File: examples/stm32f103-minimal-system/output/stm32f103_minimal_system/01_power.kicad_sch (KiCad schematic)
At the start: 8 parts, among them J1 USB-C16PIN, U2 AMS1117-3.3

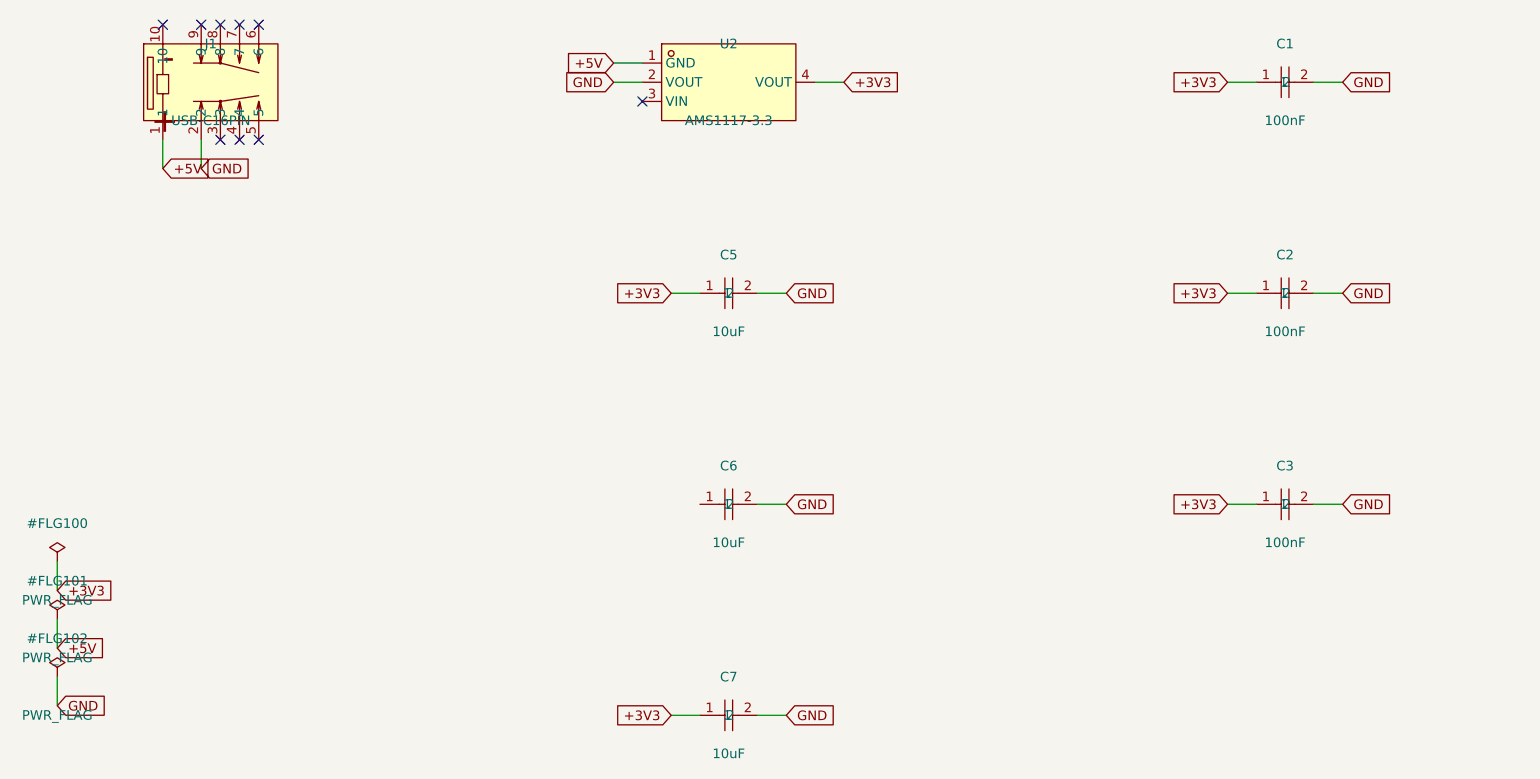
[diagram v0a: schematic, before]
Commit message: chore(example): update STM32F103 with easyeda2kicad symbols, footprints, and PCB layout 更新示例：easyeda2kicad 符号+封装、PCB 布局
- All symbols regenerated via easyeda2kicad (correct pin alignment)
- All footprints now have real pads from EasyEDA data
- Add pcb_layout.regions to circuit-model.json for agent-driven PCB placement
- Refresh schematics, reports, and operation logs from latest pipeline

Co-Authored-By: Claude Opus 4.7 <noreply@anthropic.com>
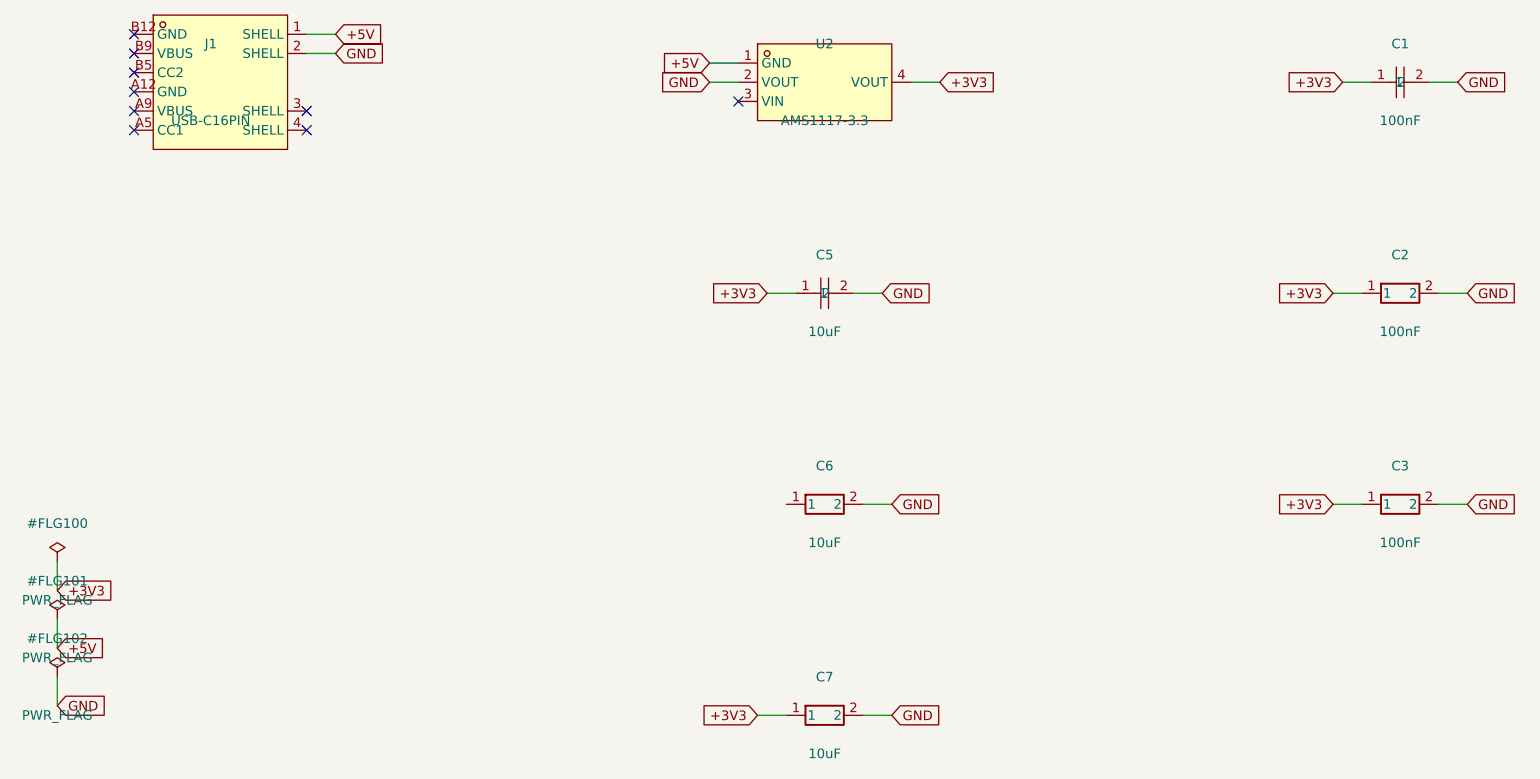
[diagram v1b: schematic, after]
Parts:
- removed C2, C3: 100nF, symbol JLC-MCP:CL10B104KA8NNNC
- removed C6, C7: 10uF, symbol JLC-MCP:CL21A106KOQNNNE
- removed J1: USB-C16PIN, symbol JLC-MCP:P-5V
- added C2, C3: 100nF, symbol JLC-MCP:C1590
- added C6, C7: 10uF, symbol JLC-MCP:C1713
- added J1: USB-C16PIN, symbol JLC-MCP:USB-TYPE-C-006
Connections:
- net +3V3: now also C2.1, C3.1, C7.1
- net +5V: now also J1.1 (SHELL)
- net GND: now also C2.2, C3.2, C6.2, C7.2, J1.2 (SHELL)
